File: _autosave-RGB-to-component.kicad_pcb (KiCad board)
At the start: 2 copper layers, 50 x 70 mm, 56 parts, among them J1 VGA, J3 USB_C_Receptacle_Power, J4 SCART_CONN, J5 3xRCA_CONN, U1 SC6206B-65K5, U2 TPF144-VR, U3 RS8752XQ, U4 TPF-141TR, U6 74AHC1G86, U7 74AHC1G86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

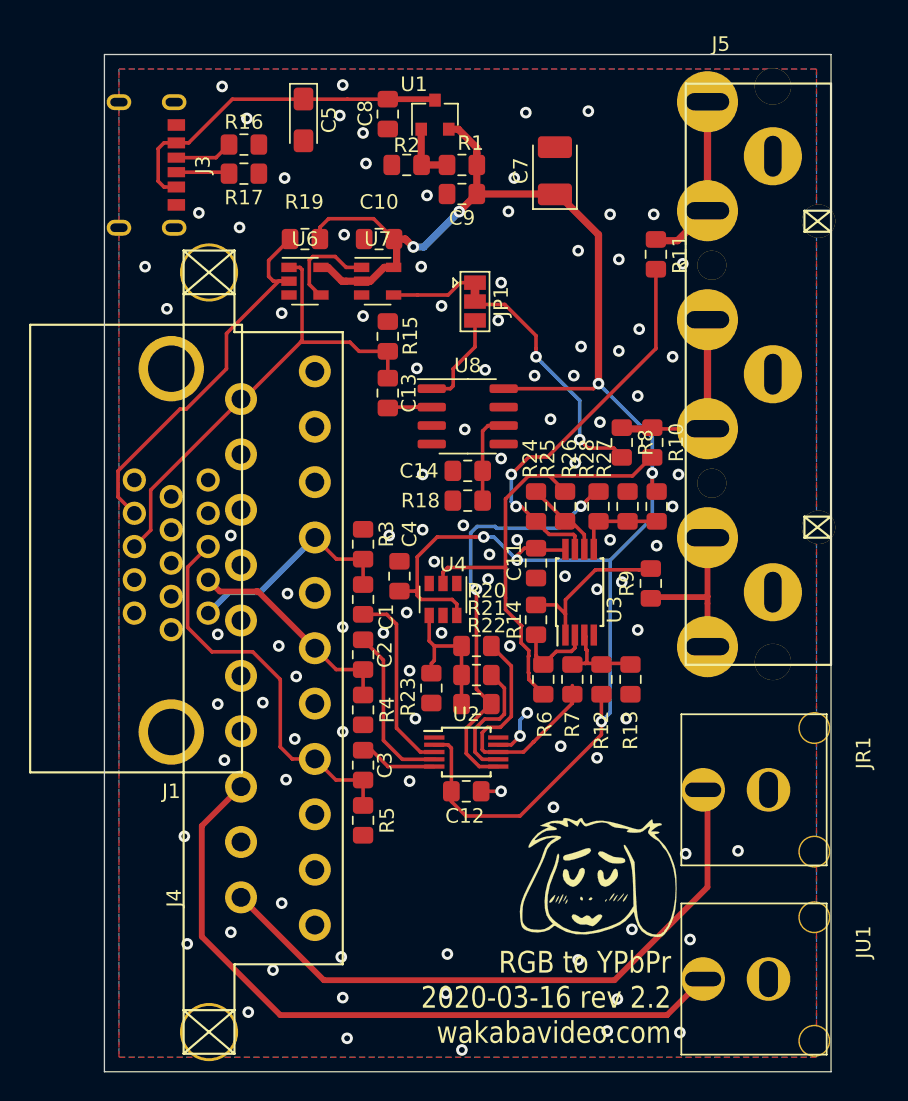
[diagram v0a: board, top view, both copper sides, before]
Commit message: reusing video amp, ferrite, power led, updated jlc files
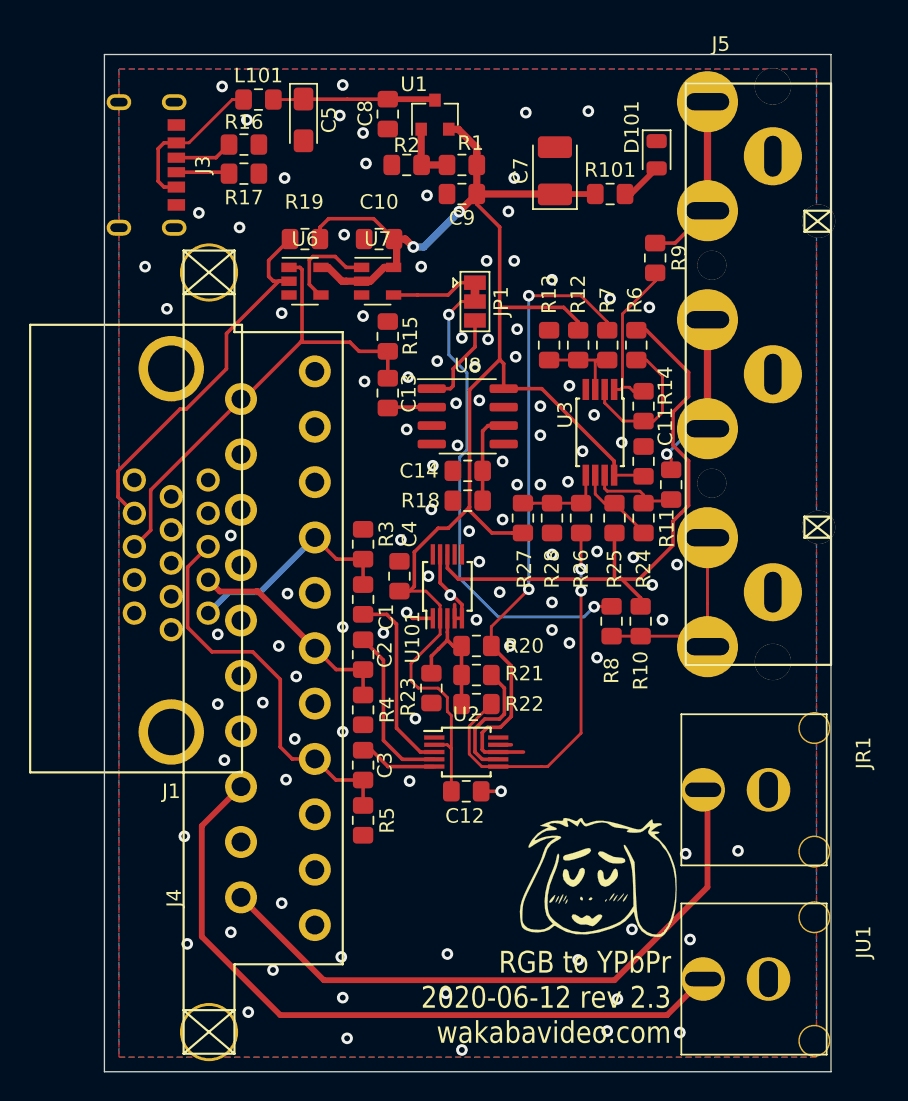
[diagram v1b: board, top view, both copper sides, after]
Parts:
- removed U4: TPF-141TR, Package_TO_SOT_SMD:SOT-23-6
- added D101: LED, LED_SMD:LED_0805_2012Metric, F.Cu at (58.0, 46.9)
- added GOTE2: Fiducial, videobits:borgar, B.Cu at (47.8, 80.7)
- added L101: 10u, Inductor_SMD:L_0805_2012Metric_Pad1.15x1.40mm_HandSolder, F.Cu at (30.6, 43.1)
- added R101: 1k, Resistor_SMD:R_0805_2012Metric_Pad1.15x1.40mm_HandSolder, F.Cu at (54.8, 49.6)
- added U101: TPF144-VR, Package_SO:MSOP-10_3x3mm_P0.5mm, F.Cu at (43.6, 76.6)
- moved R6 23.9 mm to (56.6, 60.0), turned to 270 degrees
- moved R13 23.7 mm to (50.6, 60.0), turned to 270 degrees
- moved R7 23.1 mm to (54.6, 60.0), turned to 270 degrees
- moved R12 23.1 mm to (52.6, 60.0), turned to 270 degrees
- moved R9 22.4 mm to (57.9, 54.0), turned to 270 degrees
- moved R14 16.5 mm to (57.1, 64.2)
- moved R11 15.9 mm to (59.0, 69.6)
- moved R10 12.3 mm to (56.9, 79.0), turned to 90 degrees
- moved R8 12.3 mm to (54.9, 79.0), turned to 90 degrees
- moved U3 11.1 mm to (54.1, 66.0), turned to 270 degrees
- moved C11 10.2 mm to (57.1, 68.0), turned to 90 degrees
- moved R27 9.23 mm to (48.8, 71.9), turned to 90 degrees
- moved R24 7.44 mm to (57.1, 71.9), turned to 90 degrees
- moved R28 5.26 mm to (50.8, 71.9), turned to 90 degrees
- moved R25 3.49 mm to (55.1, 71.9), turned to 90 degrees
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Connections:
- J3 pad A9: +5V -> Net-(J3-PadA9)
- J3 pad B9: +5V -> Net-(J3-PadA9)
- R10 pad 1: Net-(J5-Pad1) -> Net-(J5-Pad3)
- R11 pad 1: Net-(J5-Pad2) -> Net-(J5-Pad1)
- R8 pad 1: Net-(J5-Pad1) -> Net-(J5-Pad3)
- R9 pad 1: Net-(J5-Pad3) -> Net-(J5-Pad2)
- U2 pad 1: Net-(U2-Pad1) -> GND
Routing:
- net /2R: track 17.9 -> 43.8 mm, vias 0 -> 2
- net /2Pb: track 27.3 -> 6.31 mm, vias 2 -> 0
- net /SYNC: track 16.9 -> 32.9 mm
- net VCC: track 128.3 -> 112.6 mm, vias 7 -> 2
- net +5V: track 24.1 -> 11.2 mm
- net Net-(J3-PadA9): track 0.00 -> 10.9 mm
- net /2Y: track 32.6 -> 41.5 mm
- net GND: track 4.93 -> 10.7 mm, vias 104 -> 105
- net Net-(R14-Pad1): track 5.69 -> 10.4 mm
- net Net-(J5-Pad3): track 11.4 -> 14.4 mm
- net Net-(D101-Pad2): track 0.00 -> 2.91 mm
- net /2B: track 29.4 -> 26.8 mm
- net Net-(J5-Pad1): track 13.4 -> 12.2 mm, vias 0 -> 1
- net Net-(R20-Pad1): track 10.1 -> 9.37 mm
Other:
- net class Default: clearance 0.2 -> 0.15; trace_width 0.25 -> 0.15
- rule trace_clearance: 0.2 -> 0.15
- rule trace_min: 0.2 -> 0.15
- board text added: "RGB to YPbPr 2020-06-12 rev 2.3 wakabavideo.com"
- board text removed: "RGB to YPbPr 2020-03-16 rev 2.2 wakabavideo.com"
